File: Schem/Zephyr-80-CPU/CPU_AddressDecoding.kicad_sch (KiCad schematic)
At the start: 16 parts, among them U1 AS7C4096A-12TCN, U2 ATF22V10C-10PU, U3 Z084000xP, U4 SST39SF040-70-4C-PHE, U5 ATF22V10C-10PU, U6 SN74HC273DWR, U7 SN74HC244DWR, Y1 ECS-2100AX-100

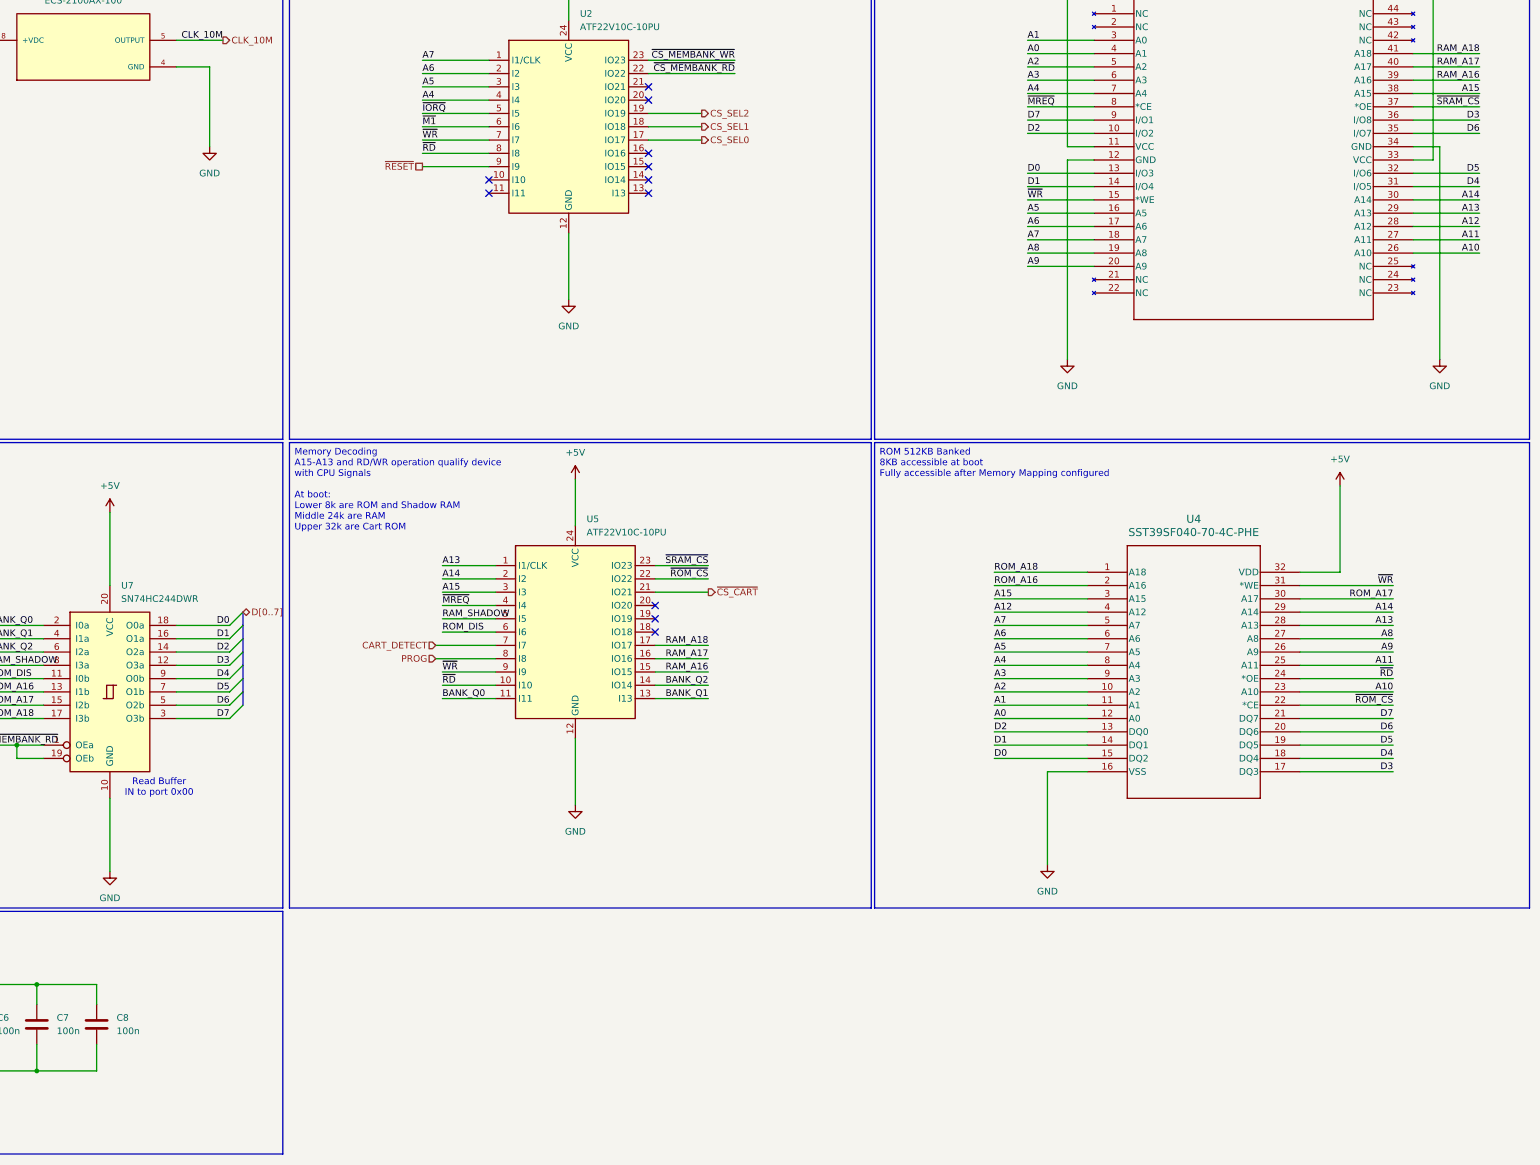
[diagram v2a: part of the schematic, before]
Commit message: Fixed memory select wiring and added bulk cap on the power input.
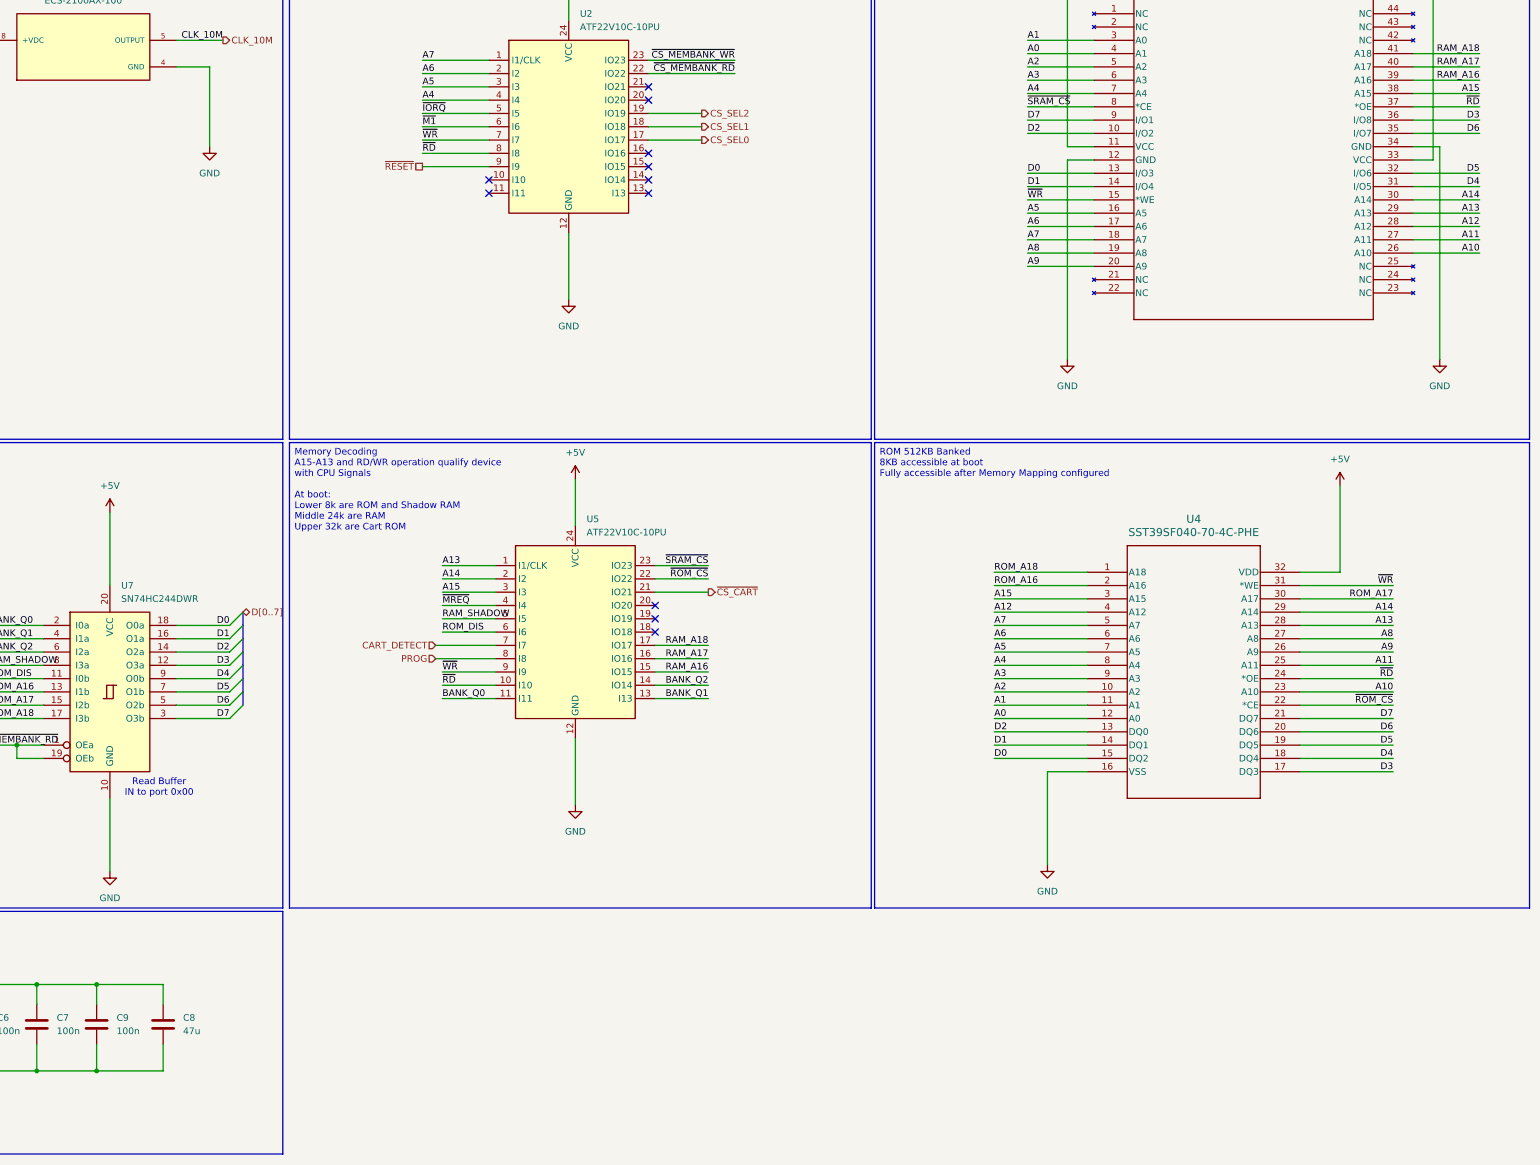
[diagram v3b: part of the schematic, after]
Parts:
- added C9: 100n, Capacitor_SMD:C_0603_1608Metric, symbol Device:C
- C8: value 100n -> 47u; footprint Capacitor_SMD:C_0603_1608Metric -> Capacitor_SMD:C_1206_3216Metric; MANUFACTURER_PART_NUMBER 0603B104K160CT -> C3216X5R1E476M160AC
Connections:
- net +5V: now also C9.1
- net GND: now also C9.2
- net ~{MREQ}: no longer U1.8 (*CE)
- net ~{RD}: now also U1.37 (*OE)
- net ~{SRAM_CS}: now also U1.8 (*CE); no longer U1.37 (*OE)
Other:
- moved on the sheet: C8
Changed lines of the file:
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@@
 	)
 	(junction
+		(at 124.46 232.41)
+		(diameter 0)
+		(color 0 0 0 0)
+	)
+	(junction
 		(at 113.03 232.41)
 		(diameter 0)
@@
 	)
 	(junction
+		(at 124.46 248.92)
+		(diameter 0)
+		(color 0 0 0 0)
+	)
+	(junction
 		(at 67.31 232.41)
 		(diameter 0)
@@
 	(wire
 		(pts
+			(xy 137.16 243.84) (xy 137.16 248.92)
+		)
+		(stroke
+			(width 0)
+			(type default)
+		)
+	)
+	(wire
+		(pts
 			(xy 354.33 191.77) (xy 372.11 191.77)
 		)
@@
 	(wire
 		(pts
+			(xy 124.46 232.41) (xy 137.16 232.41)
+		)
+		(stroke
+			(width 0)
+			(type default)
+		)
+	)
+	(wire
+		(pts
 			(xy 30.48 92.71) (xy 44.45 92.71)
 		)
@@
 	(wire
 		(pts
+			(xy 137.16 236.22) (xy 137.16 232.41)
+		)
+		(stroke
+			(width 0)
+			(type default)
+		)
+	)
+	(wire
+		(pts
 			(xy 354.33 166.37) (xy 372.11 166.37)
 		)
@@
 	(wire
 		(pts
+			(xy 124.46 248.92) (xy 137.16 248.92)
+		)
+		(stroke
+			(width 0)
+			(type default)
+		)
+	)
+	(wire
+		(pts
 			(xy 149.86 163.83) (xy 139.7 163.83)
 		)
@@
 		)
 	)
-	(label "~{MREQ}"
+	(label "~{SRAM_CS}"
 		(at 302.26 64.77 0)
 		(effects
@@
 		)
 	)
-	(label "~{SRAM_CS}"
+	(label "~{RD}"
 		(at 388.62 64.77 180)
 		(effects
@@
 	(symbol
 		(lib_id "Device:C")
+		(at 124.46 240.03 0)
+		(unit 1)
+		(exclude_from_sim no)
+		(in_bom yes)
+		(on_board yes)
+		(dnp no)
+		(fields_autoplaced yes)
+		(property "Reference" "C9"
+			(at 128.27 238.7599 0)
+			(effects
+				(font
+					(size 1.27 1.27)
+				)
+				(justify left)
+			)
+		)
+		(property "Value" "100n"
+			(at 128.27 241.2999 0)
+			(effects
+				(font
+					(size 1.27 1.27)
+				)
+				(justify left)
+			)
+		)
+		(property "Footprint" "Capacitor_SMD:C_0603_1608Metric"
+			(at 125.4252 243.84 0)
+			(effects
+				(font
+					(size 1.27 1.27)
+				)
+				(hide yes)
+			)
+		)
+		(property "Datasheet" "~"
+			(at 124.46 240.03 0)
+			(effects
+				(font
+					(size 1.27 1.27)
+				)
+				(hide yes)
+			)
+		)
+		(property "Description" "Unpolarized capacitor"
+			(at 124.46 240.03 0)
+			(effects
+				(font
+					(size 1.27 1.27)
+				)
+				(hide yes)
+			)
+		)
+		(property "KLC_S4.2_3V3OUT" ""
+			(at 124.46 240.03 0)
+			(effects
+				(font
+					(size 1.27 1.27)
+				)
+				(hide yes)
+			)
+		)
+		(property "KLC_S4.2_VCC" ""
+			(at 124.46 240.03 0)
+			(effects
+				(font
+					(size 1.27 1.27)
+				)
+				(hide yes)
+			)
+		)
+		(property "MANUFACTURER_PART_NUMBER" "0603B104K160CT"
+			(at 124.46 240.03 0)
+			(effects
+				(font
+					(size 1.27 1.27)
+				)
+				(hide yes)
+			)
+		)
+		(pin "1"
+		)
+		(pin "2"
+		)
+		(instances
+			(project "Z80HomeBrew"
+				(path "/5593e793-d133-45d0-a91e-72805049e474/42f260a1-43d6-4f51-bd99-df380e29398c"
+					(reference "C20")
+					(unit 1)
+				)
+			)
+			(project "Z80HomeBrew"
+				(path "/dc6b683c-bfa8-4cb5-a3c8-a89070b5c279/236fa83f-f78f-4d87-90cb-d181eac13394"
+					(reference "C9")
+					(unit 1)
+				)
+			)
+			(project "CPU_AddressDecoding"
+				(path "/f3536fc1-7602-4cc7-ae5a-b620f9bbf363"
+					(reference "C?")
+					(unit 1)
+				)
+			)
+		)
+	)
+	(symbol
+		(lib_id "Device:C")
 		(at 101.6 240.03 0)
 		(unit 1)
@@
 	(symbol
 		(lib_id "Device:C")
-		(at 124.46 240.03 0)
+		(at 137.16 240.03 0)
 		(unit 1)
 		(exclude_from_sim no)
@@
 		(fields_autoplaced yes)
 		(property "Reference" "C8"
-			(at 128.27 238.7599 0)
+			(at 140.97 238.7599 0)
 			(effects
 				(font
@@
 			)
 		)
-		(property "Value" "100n"
-			(at 128.27 241.2999 0)
+		(property "Value" "47u"
+			(at 140.97 241.2999 0)
 			(effects
 				(font
@@
 			)
 		)
-		(property "Footprint" "Capacitor_SMD:C_0603_1608Metric"
-			(at 125.4252 243.84 0)
+		(property "Footprint" "Capacitor_SMD:C_1206_3216Metric"
+			(at 138.1252 243.84 0)
 			(effects
 				(font
@@
 		)
 		(property "Datasheet" "~"
-			(at 124.46 240.03 0)
+			(at 137.16 240.03 0)
 			(effects
 				(font
@@
 		)
 		(property "Description" "Unpolarized capacitor"
-			(at 124.46 240.03 0)
+			(at 137.16 240.03 0)
 			(effects
 				(font
@@
 		)
 		(property "KLC_S4.2_3V3OUT" ""
-			(at 124.46 240.03 0)
+			(at 137.16 240.03 0)
 			(effects
 				(font
@@
 		)
 		(property "KLC_S4.2_VCC" ""
-			(at 124.46 240.03 0)
+			(at 137.16 240.03 0)
 			(effects
 				(font
@@
 			)
 		)
-		(property "MANUFACTURER_PART_NUMBER" "0603B104K160CT"
-			(at 124.46 240.03 0)
+		(property "MANUFACTURER_PART_NUMBER" "C3216X5R1E476M160AC"
+			(at 137.16 240.03 0)
 			(effects
 				(font
@@
 		)
 		(instances
-			(project "Z80HomeBrew"
-				(path "/5593e793-d133-45d0-a91e-72805049e474/42f260a1-43d6-4f51-bd99-df380e29398c"
-					(reference "C20")
-					(unit 1)
-				)
-			)
-			(project "Z80HomeBrew"
+			(project "Zephyr-80-CPU"
 				(path "/dc6b683c-bfa8-4cb5-a3c8-a89070b5c279/236fa83f-f78f-4d87-90cb-d181eac13394"
 					(reference "C8")
 					(unit 1)
 				)
-			)
-			(project "CPU_AddressDecoding"
-				(path "/f3536fc1-7602-4cc7-ae5a-b620f9bbf363"
-					(reference "C?")
-					(unit 1)
-				)
